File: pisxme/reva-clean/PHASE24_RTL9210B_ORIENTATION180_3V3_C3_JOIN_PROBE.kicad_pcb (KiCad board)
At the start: 6 copper layers, 80 x 45 mm, 12 parts, among them J1 M.2 Socket 3 M-key 2280, U1 RTL9210B-CG, U2 W25Q128_SPI_FLASH, Y1 XTAL_25MHz

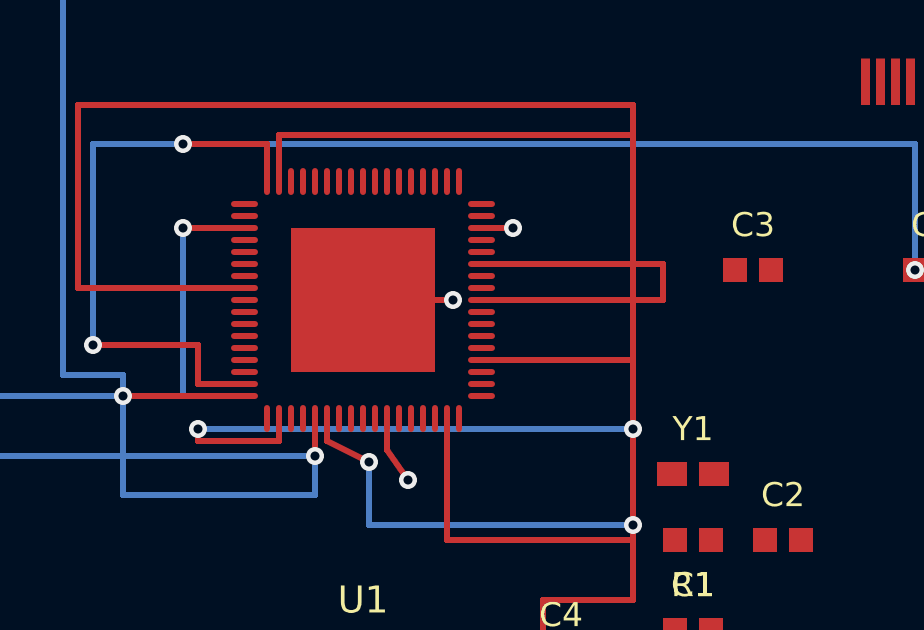
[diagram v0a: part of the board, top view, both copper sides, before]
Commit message: complete RTL9210B 3V3 physical field
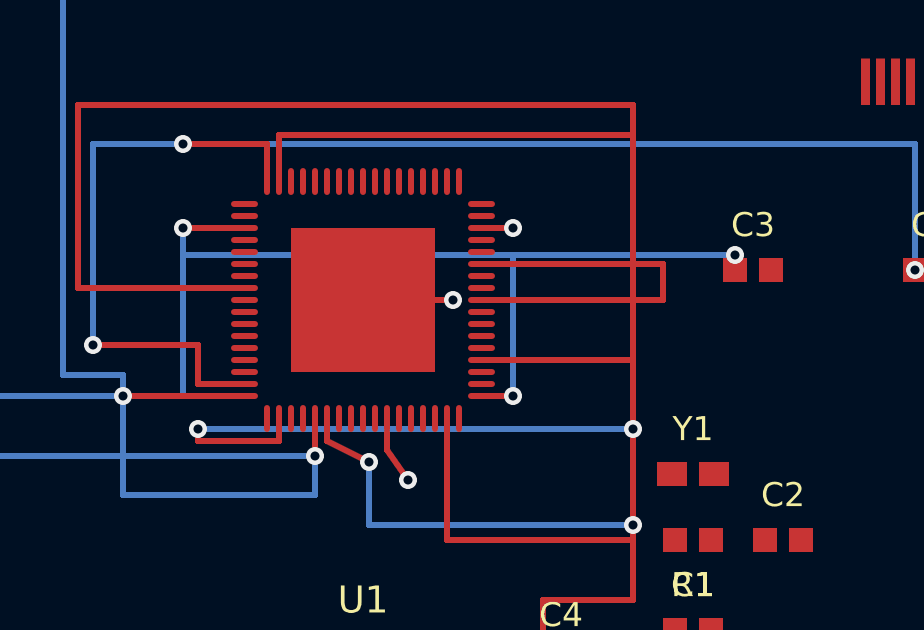
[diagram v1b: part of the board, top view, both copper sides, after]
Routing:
- net RTL_3V3: track 98.0 -> 123.5 mm, vias 7 -> 9
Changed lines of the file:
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@@
+	)
+	(segment
+		(start 101.95 73.2)
+		(end 103 73.2)
+		(width 0.2)
+		(layer "F.Cu")
+		(net "RTL_3V3")
+	)
+	(segment
+		(start 110.4 68.5)
+		(end 110.4 69)
+		(width 0.2)
+		(layer "F.Cu")
+		(net "RTL_3V3")
 	)
 	(segment
@@
 	)
 	(via
+		(at 110.4 68.5)
+		(size 0.6)
+		(drill 0.3)
+		(layers "F.Cu" "B.Cu")
+		(net "RTL_3V3")
+	)
+	(via
 		(at 90 73.2)
 		(size 0.6)
@@
 		(net "RTL_3V3")
 	)
+	(via
+		(at 103 73.2)
+		(size 0.6)
+		(drill 0.3)
+		(layers "F.Cu" "B.Cu")
+		(net "RTL_3V3")
+	)
 	(segment
 		(start 90 72.5)
 		(end 90 73.2)
+		(width 0.2)
+		(layer "B.Cu")
+		(net "RTL_3V3")
+	)
+	(segment
+		(start 103 68.5)
+		(end 110.4 68.5)
 		(width 0.2)
 		(layer "B.Cu")
@@
 		(start 93.2 57)
 		(end 88 57)
+		(width 0.2)
+		(layer "B.Cu")
+		(net "RTL_3V3")
+	)
+	(segment
+		(start 103 73.2)
+		(end 103 68.5)
 		(width 0.2)
 		(layer "B.Cu")
@@
 		(width 0.2)
 		(layer "B.Cu")
+		(net "RTL_3V3")
+	)
+	(segment
+		(start 103 68.5)
+		(end 92 68.5)
+		(width 0.2)
+		(layer "B.Cu")
+		(net "RTL_3V3")
+	)
+	(segment
+		(start 92 68.5)
+		(end 92 67.6)
+		(width 0.2)
+		(layer "B.Cu")
